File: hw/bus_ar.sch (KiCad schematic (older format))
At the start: 5 parts, among them U901 74HC573, U902 74HC573, U903 74HC245, U904 74HC574, U905 74HC574

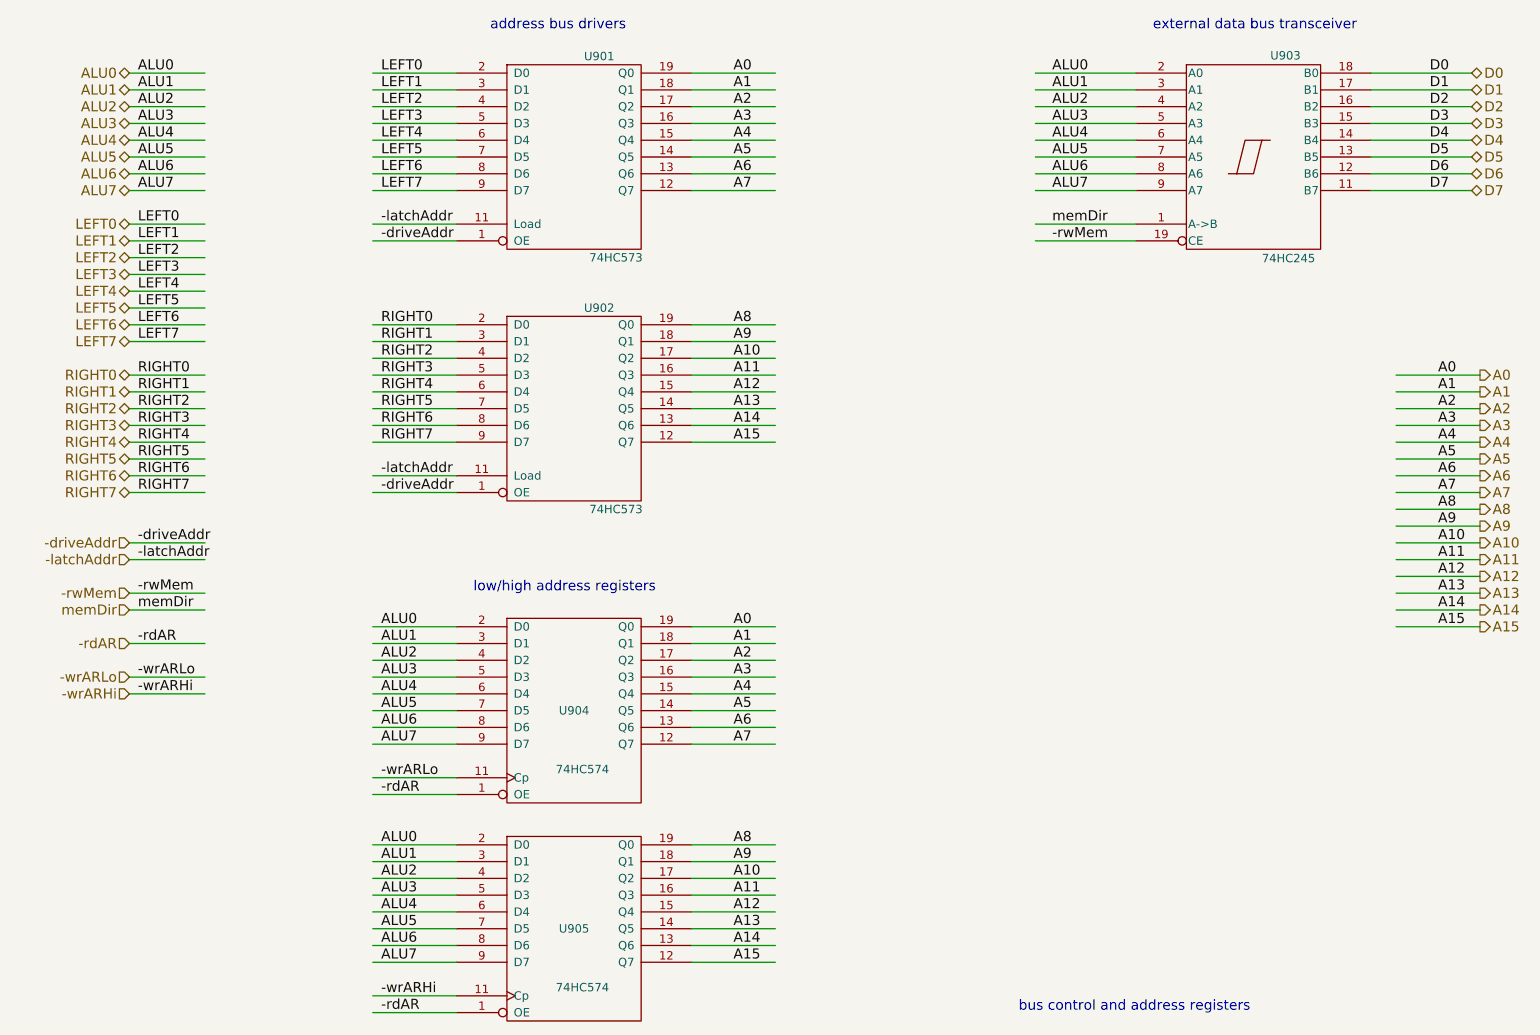
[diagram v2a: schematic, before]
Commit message: remove AR registers, switch to new ucode impl
Note that there is a bug in the ucode module:
the -uExtW and -uExtR signals are generated incorrectly.
(They need to be OR gates, not AND gates, so that
they can be held high when -uExtRW is not asserted.)
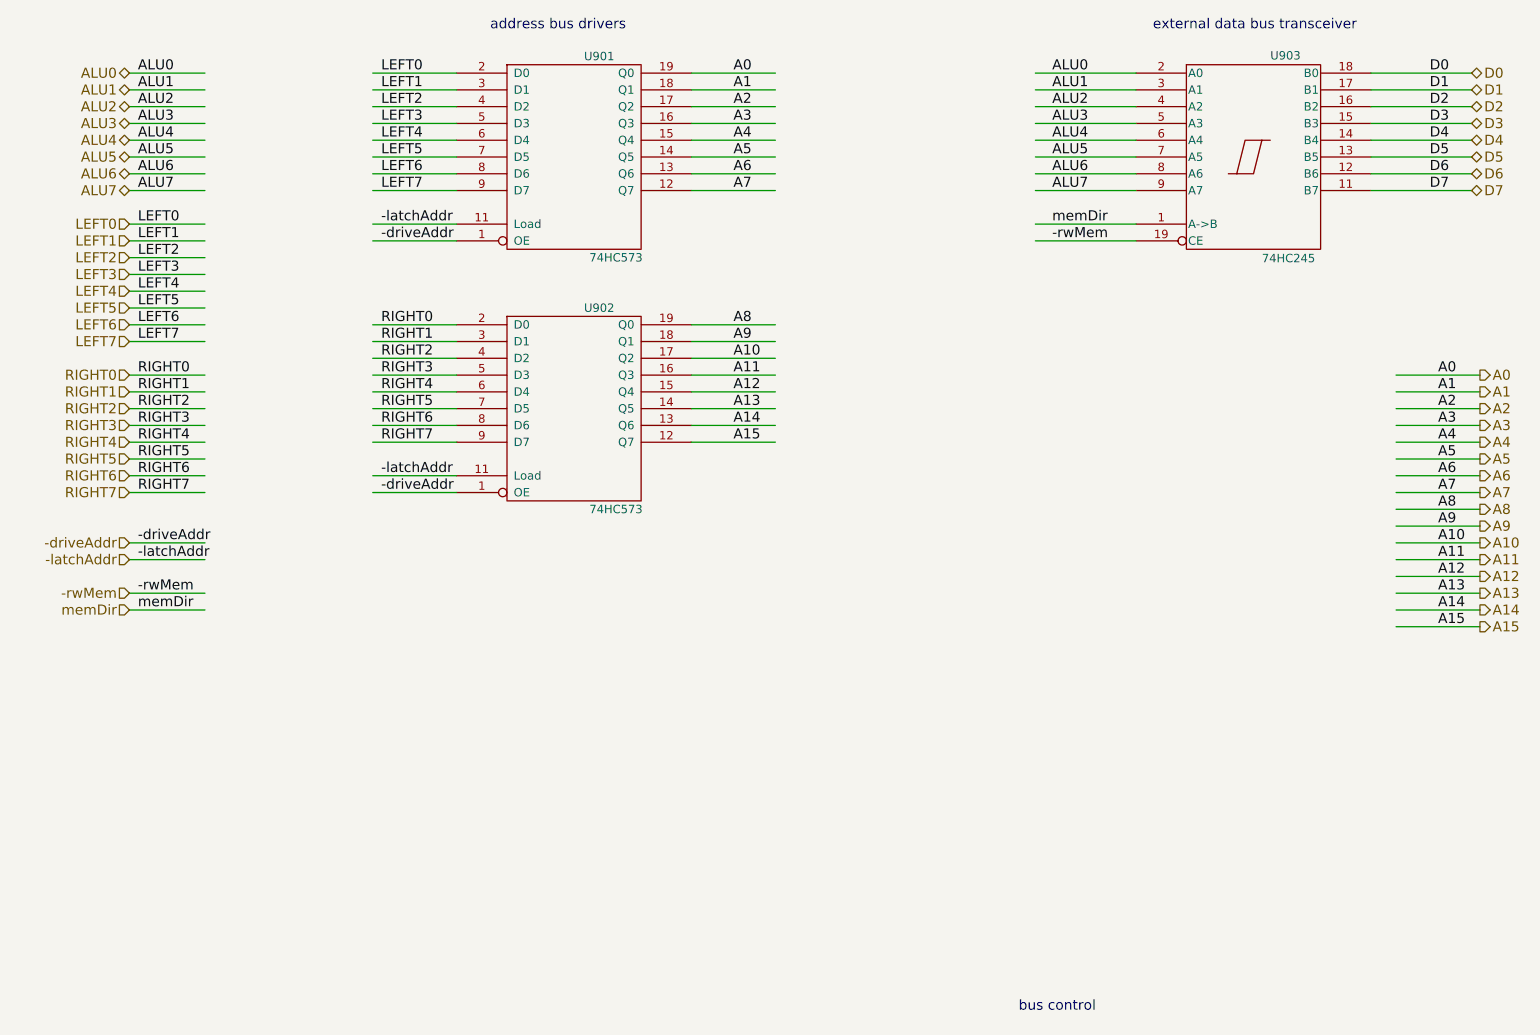
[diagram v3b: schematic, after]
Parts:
- removed U904, U905: 74HC574, symbol 74LS574
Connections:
- net labels removed: -rdAR, -wrARHi, -wrARLo
- wire segments 137 -> 98
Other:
- note added: "bus control"
- note removed: "bus control and address registers"
- note removed: "low/high address registers"
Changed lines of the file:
@@
 $EndDescr
 Text Notes 7150 6800 0    60   ~ 0
-bus control and address registers
+bus control
 Wire Wire Line
 	3800 1200 3300 1200
@@
 Text Label 9600 1900 0    60   ~ 0
 D7
-$Comp
-L 74LS574 U904
-U 1 1 595F244F
-P 4500 5000
-F 0 "U904" H 4500 5000 50  0000 C CNN
-F 1 "74HC574" H 4550 4650 50  0000 C CNN
-F 2 "" H 4500 5000 50  0001 C CNN
-F 3 "" H 4500 5000 50  0001 C CNN
-	1    4500 5000
-	1    0    0    -1
-$EndComp
-$Comp
-L 74LS574 U905
-U 1 1 595F246E
-P 4500 6300
-F 0 "U905" H 4500 6300 50  0000 C CNN
-F 1 "74HC574" H 4550 5950 50  0000 C CNN
-F 2 "" H 4500 6300 50  0001 C CNN
-F 3 "" H 4500 6300 50  0001 C CNN
-	1    4500 6300
-	1    0    0    -1
-$EndComp
-Wire Wire Line
-	3800 4500 3300 4500
-Wire Wire Line
-	3800 4600 3300 4600
-Wire Wire Line
-	3800 4700 3300 4700
-Wire Wire Line
-	3800 4800 3300 4800
-Wire Wire Line
-	3800 4900 3300 4900
-Wire Wire Line
-	3800 5000 3300 5000
-Wire Wire Line
-	3800 5100 3300 5100
-Wire Wire Line
-	3800 5200 3300 5200
-Wire Wire Line
-	3800 5800 3300 5800
-Wire Wire Line
-	3800 5900 3300 5900
-Wire Wire Line
-	3800 6000 3300 6000
-Wire Wire Line
-	3800 6100 3300 6100
-Wire Wire Line
-	3800 6200 3300 6200
-Wire Wire Line
-	3800 6300 3300 6300
-Wire Wire Line
-	3800 6400 3300 6400
-Wire Wire Line
-	3800 6500 3300 6500
-Text Label 3350 4500 0    60   ~ 0
-ALU0
-Text Label 3350 4600 0    60   ~ 0
-ALU1
-Text Label 3350 4700 0    60   ~ 0
-ALU2
-Text Label 3350 4800 0    60   ~ 0
-ALU3
-Text Label 3350 4900 0    60   ~ 0
-ALU4
-Text Label 3350 5000 0    60   ~ 0
-ALU5
-Text Label 3350 5100 0    60   ~ 0
-ALU6
-Text Label 3350 5200 0    60   ~ 0
-ALU7
-Text Label 3350 5800 0    60   ~ 0
-ALU0
-Text Label 3350 5900 0    60   ~ 0
-ALU1
-Text Label 3350 6000 0    60   ~ 0
-ALU2
-Text Label 3350 6100 0    60   ~ 0
-ALU3
-Text Label 3350 6200 0    60   ~ 0
-ALU4
-Text Label 3350 6300 0    60   ~ 0
-ALU5
-Text Label 3350 6400 0    60   ~ 0
-ALU6
-Text Label 3350 6500 0    60   ~ 0
-ALU7
 Wire Wire Line
 	1850 1200 2300 1200
@@
 Wire Wire Line
 	1850 4400 2300 4400
-Wire Wire Line
-	1850 4600 2300 4600
-Wire Wire Line
-	1850 4800 2300 4800
-Wire Wire Line
-	1850 4900 2300 4900
 Text Label 1900 4000 0    60   ~ 0
 -driveAddr
@@
 Text Label 1900 4400 0    60   ~ 0
 memDir
-Wire Wire Line
-	3800 5400 3300 5400
-Wire Wire Line
-	3800 5500 3300 5500
-Wire Wire Line
-	3800 6700 3300 6700
-Wire Wire Line
-	3800 6800 3300 6800
-Text Label 3350 5400 0    60   ~ 0
--wrARLo
-Text Label 3350 5500 0    60   ~ 0
--rdAR
-Text Label 3350 6700 0    60   ~ 0
--wrARHi
-Text Label 3350 6800 0    60   ~ 0
--rdAR
-Text Label 1900 4600 0    60   ~ 0
--rdAR
-Text Label 1900 4800 0    60   ~ 0
--wrARLo
-Text Label 1900 4900 0    60   ~ 0
--wrARHi
 Text HLabel 1850 1200 0    60   BiDi ~ 0
 ALU0
@@
 Text HLabel 1850 1900 0    60   BiDi ~ 0
 ALU7
-Text HLabel 1850 2100 0    60   BiDi ~ 0
+Text HLabel 1850 2100 0    60   Input ~ 0
 LEFT0
-Text HLabel 1850 2200 0    60   BiDi ~ 0
+Text HLabel 1850 2200 0    60   Input ~ 0
 LEFT1
-Text HLabel 1850 2300 0    60   BiDi ~ 0
+Text HLabel 1850 2300 0    60   Input ~ 0
 LEFT2
-Text HLabel 1850 2400 0    60   BiDi ~ 0
+Text HLabel 1850 2400 0    60   Input ~ 0
 LEFT3
-Text HLabel 1850 2500 0    60   BiDi ~ 0
+Text HLabel 1850 2500 0    60   Input ~ 0
 LEFT4
-Text HLabel 1850 2600 0    60   BiDi ~ 0
+Text HLabel 1850 2600 0    60   Input ~ 0
 LEFT5
-Text HLabel 1850 2700 0    60   BiDi ~ 0
+Text HLabel 1850 2700 0    60   Input ~ 0
 LEFT6
-Text HLabel 1850 2800 0    60   BiDi ~ 0
+Text HLabel 1850 2800 0    60   Input ~ 0
 LEFT7
-Text HLabel 1850 3000 0    60   BiDi ~ 0
+Text HLabel 1850 3000 0    60   Input ~ 0
 RIGHT0
-Text HLabel 1850 3100 0    60   BiDi ~ 0
+Text HLabel 1850 3100 0    60   Input ~ 0
 RIGHT1
-Text HLabel 1850 3200 0    60   BiDi ~ 0
+Text HLabel 1850 3200 0    60   Input ~ 0
 RIGHT2
-Text HLabel 1850 3300 0    60   BiDi ~ 0
+Text HLabel 1850 3300 0    60   Input ~ 0
 RIGHT3
-Text HLabel 1850 3400 0    60   BiDi ~ 0
+Text HLabel 1850 3400 0    60   Input ~ 0
 RIGHT4
-Text HLabel 1850 3500 0    60   BiDi ~ 0
+Text HLabel 1850 3500 0    60   Input ~ 0
 RIGHT5
-Text HLabel 1850 3600 0    60   BiDi ~ 0
+Text HLabel 1850 3600 0    60   Input ~ 0
 RIGHT6
-Text HLabel 1850 3700 0    60   BiDi ~ 0
+Text HLabel 1850 3700 0    60   Input ~ 0
 RIGHT7
 Text HLabel 1850 4000 0    60   Input ~ 0
@@
 Text HLabel 1850 4400 0    60   Input ~ 0
 memDir
-Text HLabel 1850 4600 0    60   Input ~ 0
--rdAR
-Text HLabel 1850 4800 0    60   Input ~ 0
--wrARLo
-Text HLabel 1850 4900 0    60   Input ~ 0
--wrARHi
 Text HLabel 9900 3000 2    60   Output ~ 0
 A0
@@
 Text Notes 7950 950  0    60   ~ 0
 external data bus transceiver
-Text Notes 3900 4300 0    60   ~ 0
-low/high address registers
-Wire Wire Line
-	5200 4500 5700 4500
-Wire Wire Line
-	5200 4600 5700 4600
-Wire Wire Line
-	5200 4700 5700 4700
-Wire Wire Line
-	5200 4800 5700 4800
-Wire Wire Line
-	5200 4900 5700 4900
-Wire Wire Line
-	5200 5000 5700 5000
-Wire Wire Line
-	5200 5100 5700 5100
-Wire Wire Line
-	5200 5200 5700 5200
-Wire Wire Line
-	5200 5800 5700 5800
-Wire Wire Line
-	5200 5900 5700 5900
-Wire Wire Line
-	5200 6000 5700 6000
-Wire Wire Line
-	5200 6100 5700 6100
-Wire Wire Line
-	5200 6200 5700 6200
-Wire Wire Line
-	5200 6300 5700 6300
-Wire Wire Line
-	5200 6400 5700 6400
-Wire Wire Line
-	5200 6500 5700 6500
-Text Label 5450 4500 0    60   ~ 0
-A0
-Text Label 5450 4600 0    60   ~ 0
-A1
-Text Label 5450 4700 0    60   ~ 0
-A2
-Text Label 5450 4800 0    60   ~ 0
-A3
-Text Label 5450 4900 0    60   ~ 0
-A4
-Text Label 5450 5000 0    60   ~ 0
-A5
-Text Label 5450 5100 0    60   ~ 0
-A6
-Text Label 5450 5200 0    60   ~ 0
-A7
-Text Label 5450 5800 0    60   ~ 0
-A8
-Text Label 5450 5900 0    60   ~ 0
-A9
-Text Label 5450 6000 0    60   ~ 0
-A10
-Text Label 5450 6100 0    60   ~ 0
-A11
-Text Label 5450 6200 0    60   ~ 0
-A12
-Text Label 5450 6300 0    60   ~ 0
-A13
-Text Label 5450 6400 0    60   ~ 0
-A14
-Text Label 5450 6500 0    60   ~ 0
-A15
 Wire Wire Line
 	9400 3000 9900 3000
